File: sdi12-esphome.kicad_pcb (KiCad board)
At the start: 2 copper layers, 86.4 x 71.1 mm, 24 parts, among them J1 SDI-12 A, J2 SDI-12 B, J3 SDI-12 C, J4 SDI-12 D, J5 Grounding, Q1 2N7002, U1 ESP32_NODEMCU, U2 74LVC1G125, U3 MCP1661

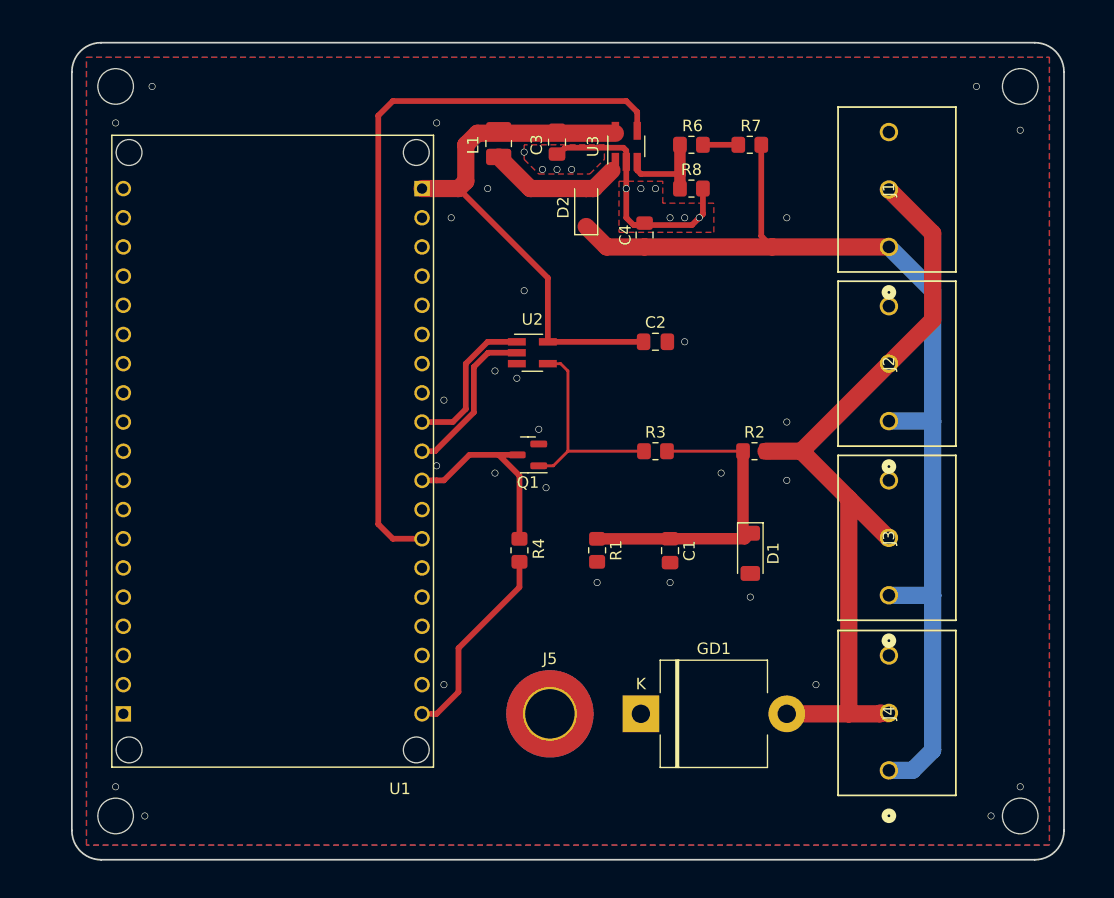
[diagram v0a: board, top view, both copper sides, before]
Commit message: board: Resize Board to fit Case, add Silkscreen Descriptions & Artwork
* Fits into BOPLA EM 212 (62212000) 100x100 mm Case
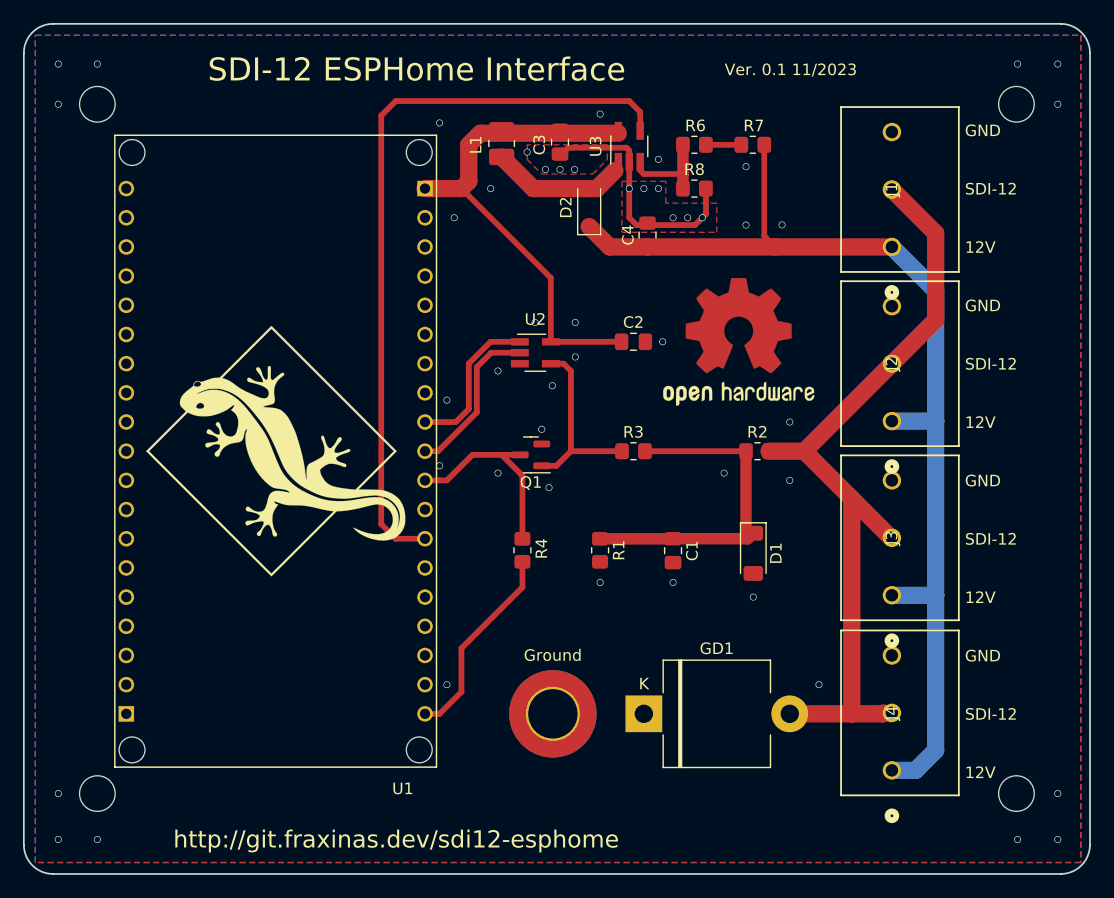
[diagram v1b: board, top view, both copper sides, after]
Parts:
- added G***: LOGO, Fraxinas:repairfox, F.Cu at (83.1, 76.5)
- added G***: LOGO, Fraxinas:purplegecko, F.Cu at (60.9, 76.2)
- added LOGO1: Logo_Open_Hardware_Small, Fraxinas:OSHW-Logo2_14.6x12mm_Mask, F.Cu at (101.2, 66.7)
- moved C2 1.92 mm to (92.1, 66.7)
- moved R3 1.92 mm to (92.1, 76.2)
- moved C1 0.26 mm to (95.5, 84.9)
- moved C3 0.26 mm to (85.7, 49.3)
- moved C4 0.26 mm to (93.3, 57.4)
- moved D1 0.26 mm to (102.5, 85.1)
- moved GD1 0.26 mm to (93.0, 99.1)
- moved J1 0.26 mm to (114.6, 58.4)
- moved J2 0.26 mm to (114.6, 73.6)
- moved J3 0.26 mm to (114.6, 88.7)
- moved J4 0.26 mm to (114.6, 104.0)
- moved L1 0.26 mm to (80.6, 49.4)
- moved Q1 0.26 mm to (83.1, 76.5)
- moved R2 0.26 mm to (102.9, 76.2)
- moved R4 0.26 mm to (82.4, 84.8)
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- renumbered J5 to Ground
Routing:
- net Net-(Q1-G): track 18.7 -> 16.5 mm
- net Net-(D1-K): track 28.0 -> 30.2 mm
- net +5V: track 45.6 -> 43.4 mm
- net GND: vias 39 -> 49
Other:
- board size 86.4 x 71.1 mm -> 92.8 x 74 mm
- board text added: "12V"
- board text added: "GND"
- board text added: "SDI-12"
- board text added: "SDI-12 ESPHome Interface"
- board text added: "Ver. 0.1 11/2023"
- board text added: "http://git.fraxinas.dev/sdi12-esphome"
